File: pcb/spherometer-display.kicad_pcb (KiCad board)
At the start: 2 copper layers, 34 x 12.2 mm, 14 parts, among them J1 Battery, J2 Indicator, J3 Disp, J4 Programming, Q1 NPN, Q2 NPN, SW1 UI-Button, U1 ATTINY85V-10SU

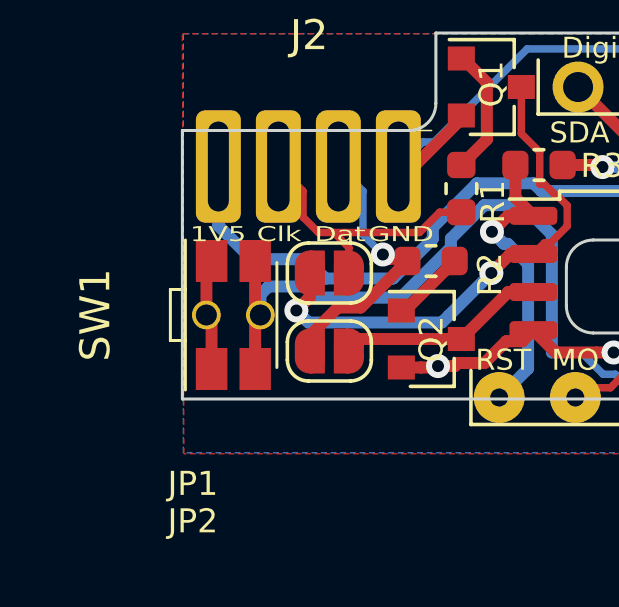
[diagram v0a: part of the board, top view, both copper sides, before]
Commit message: Bring switch closer to the edge.
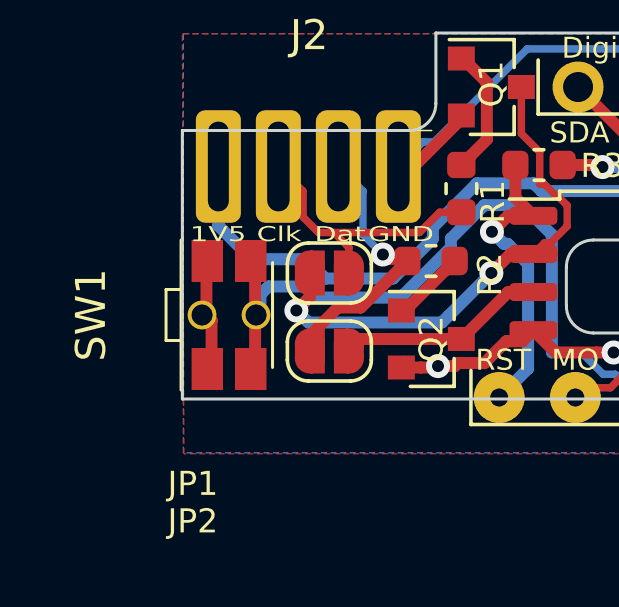
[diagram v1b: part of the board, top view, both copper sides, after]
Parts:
- moved SW1 0.14 mm to (67.1, 66.4)
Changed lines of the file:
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@@
-(kicad_pcb (version 20171130) (host pcbnew "(5.1.2-12-g89d39cf8f-dirty)")
+(kicad_pcb (version 20171130) (host pcbnew "(5.1.2-13-gd94b8b9c0-dirty)")
   (general
     (thickness 0.8)
@@
     (pad_to_mask_clearance 0)
     (aux_axis_origin 0 0)
-    (visible_elements FFFDFF7F)
+    (visible_elements FFFDEF7F)
     (pcbplotparams
       (layerselection 0x010fc_ffffffff)
@@
   )
   (module digi-spherometer:EVQP7-Switch (layer F.Cu)
-    (at 67.2 66.4 90)
+    (at 67.056 66.4 90)
     (fp_text reference SW1 (at 0 -4.6 90) (layer F.SilkS)
       (effects (font (size 1 1) (thickness 0.15)))

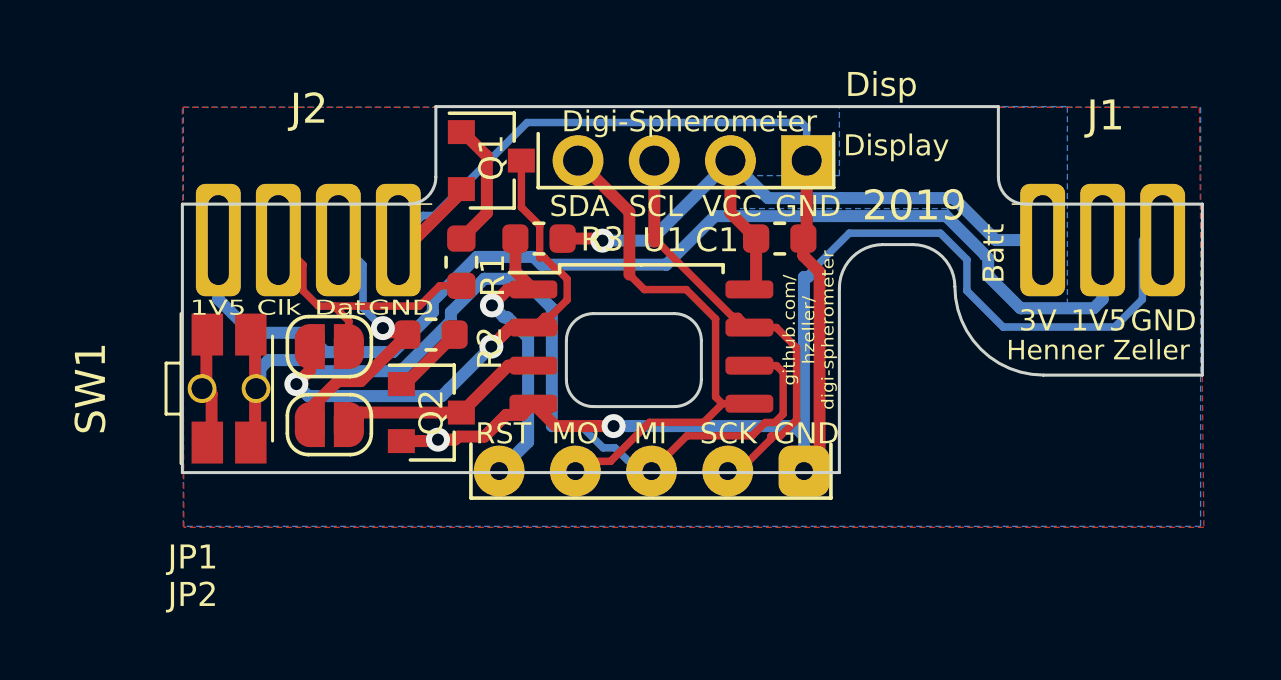
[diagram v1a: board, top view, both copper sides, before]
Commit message: Update to current KiCAD
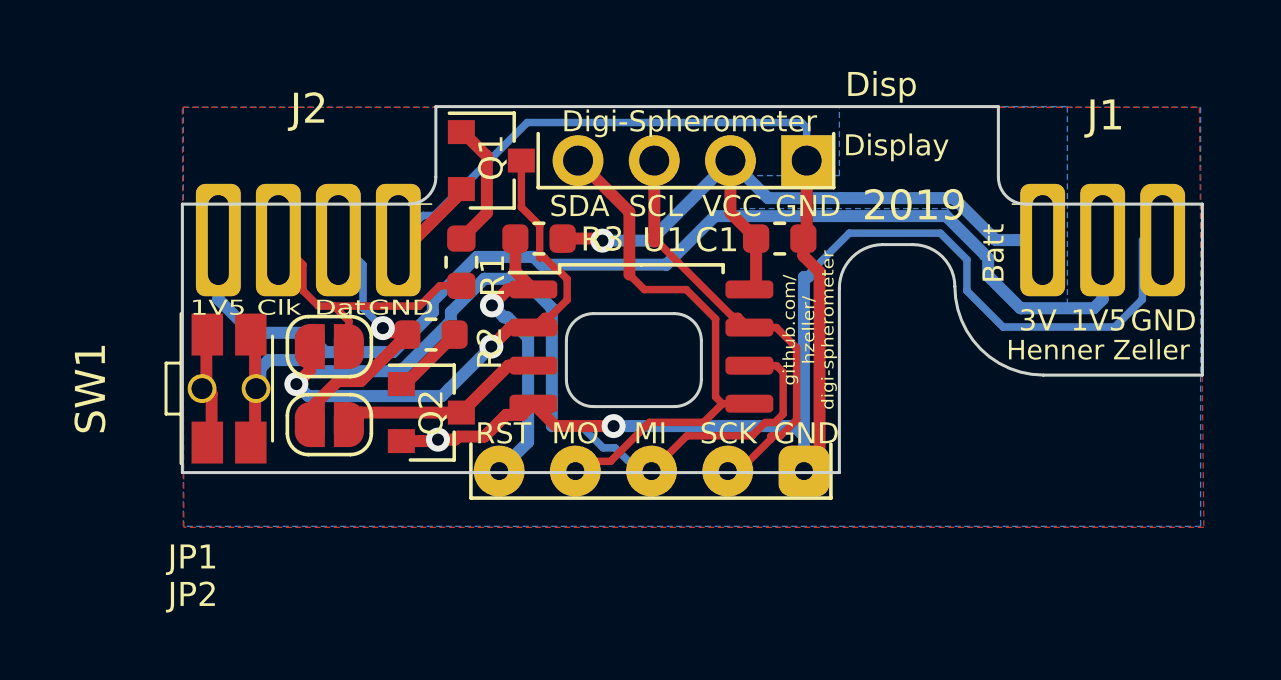
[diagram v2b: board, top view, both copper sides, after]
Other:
- outline, holes or cut-outs redrawn
- net class Default removed
